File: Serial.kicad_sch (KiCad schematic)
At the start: 19 parts

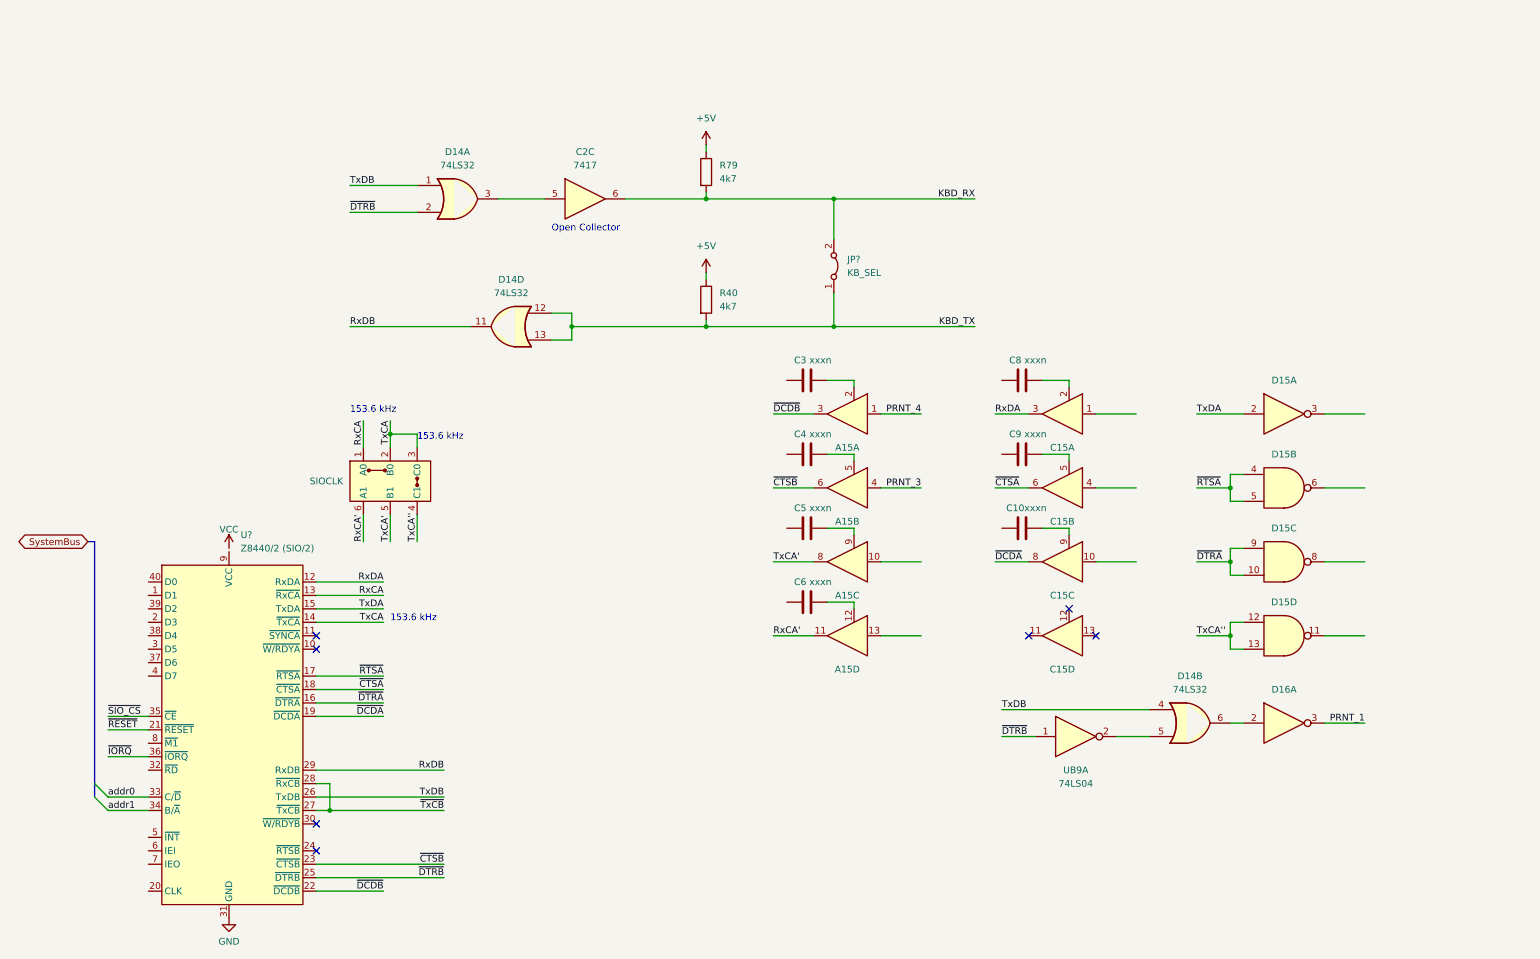
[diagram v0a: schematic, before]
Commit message: serial: wire renaming
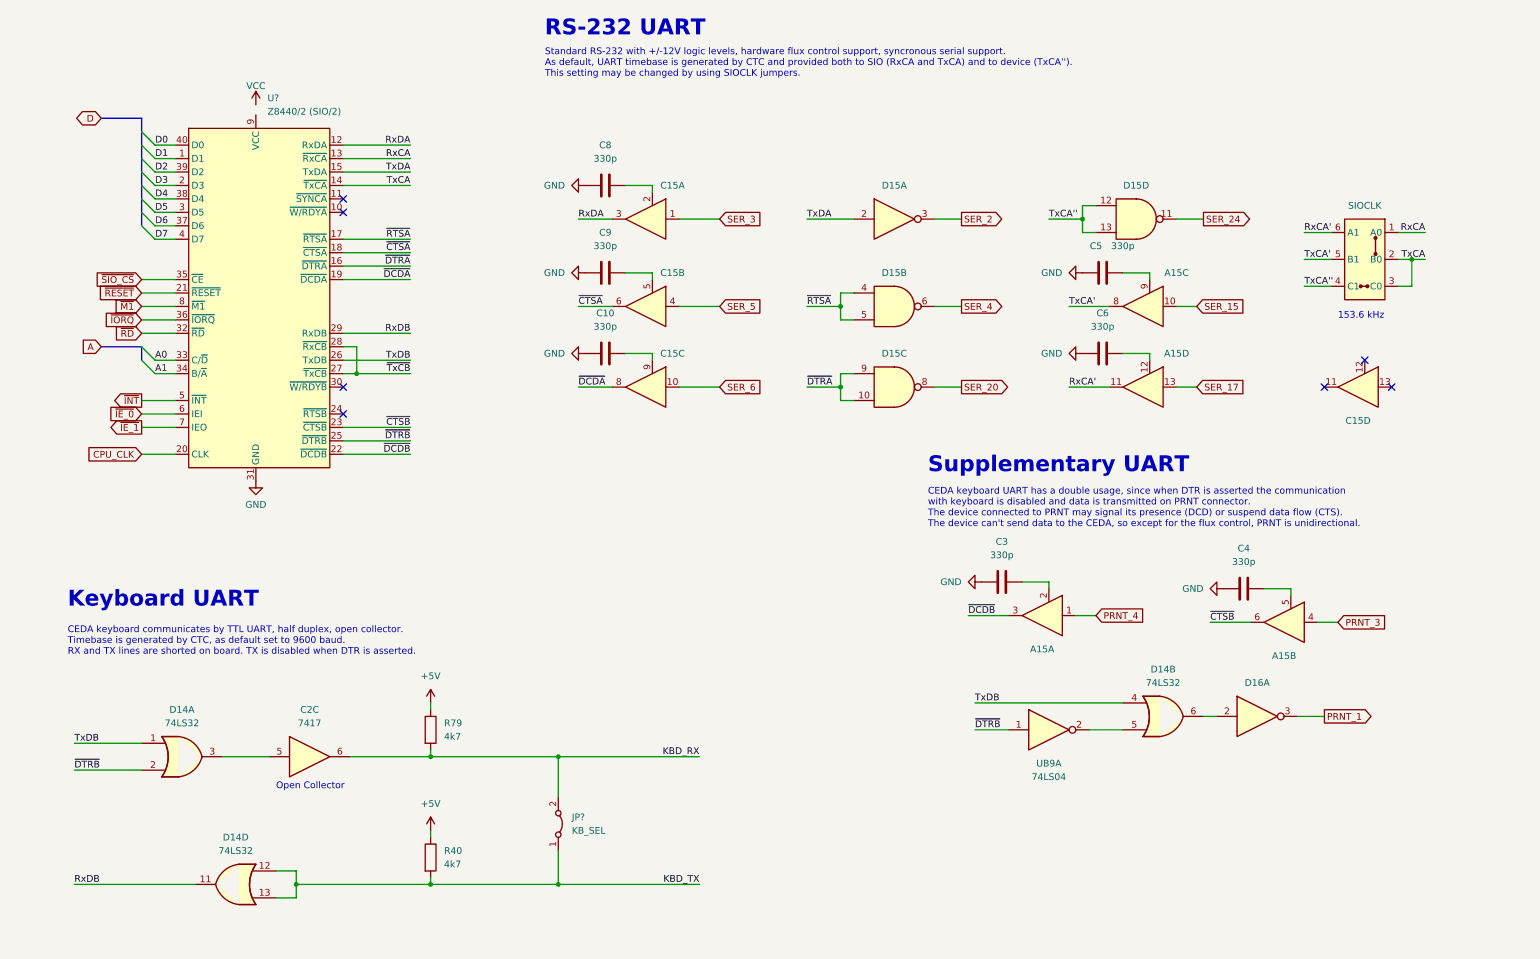
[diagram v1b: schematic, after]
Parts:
- C10, C3, C4, C5, C6, C8, C9: value xxxn -> 330p
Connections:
- net GND: now also C10.1, C3.1, C4.1, C5.1, C6.1, C8.1, C9.1
- net SER_20: now reaches D15.8
- net SER_6: now reaches C15.10
- net SER_17: now reaches A15.13
- net SER_15: now reaches A15.10
- net D1: now reaches U?.1 (D1)
- net D3: now reaches U?.2 (D3)
- net CPU_CLK: now reaches U?.20 (CLK)
- net D5: now reaches U?.3 (D5)
- net ~{RD}: now reaches U?.32 (~{RD})
- net D6: now reaches U?.37 (D6)
- net D4: now reaches U?.38 (D4)
- net D2: now reaches U?.39 (D2)
- net D7: now reaches U?.4 (D7)
- net D0: now reaches U?.40 (D0)
- net ~{INT}: now reaches U?.5 (~{INT})
- net ~{IE_0}: now reaches U?.6 (IEI)
- net ~{IE_1}: now reaches U?.7 (IEO)
- net ~{M1}: now reaches U?.8 (~{M1})
- net SER_2: now reaches D15.3
- net SER_4: now reaches D15.6
- net SER_24: now reaches D15.11
- net SER_5: now reaches C15.4
- net SER_3: now reaches C15.1
- net addr0 renamed A0
- net addr1 renamed A1
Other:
- note added: "CEDA keyboard UART has a double usage, since when DTR is asserted the communication with keyboard is disabled and data is transmitted on PRNT connector. The device connected to PRNT may signal its presence (DCD) or suspend data flow (CTS). The device can't send data to the CEDA, so except for the flux control, PRNT is unidirectional."
- note added: "CEDA keyboard communicates by TTL UART, half duplex, open collector. Timebase is generated by CTC, as default set to 9600 baud. RX and TX lines are shorted on board. TX is disabled when DTR is asserted."
- note added: "Keyboard UART"
- note added: "RS-232 UART"
- note added: "Standard RS-232 with +/-12V logic levels, hardware flux control support, syncronous serial support. As default, UART timebase is generated by CTC and provided both to SIO (RxCA and TxCA) and to device (TxCA''). This setting may be changed by using SIOCLK jumpers."
- note added: "Supplementary UART"
- moved on the sheet: A15A, A15B, A15C, A15D, C10, C15A, C15B, C15C, C15D, C2C, C3, C4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

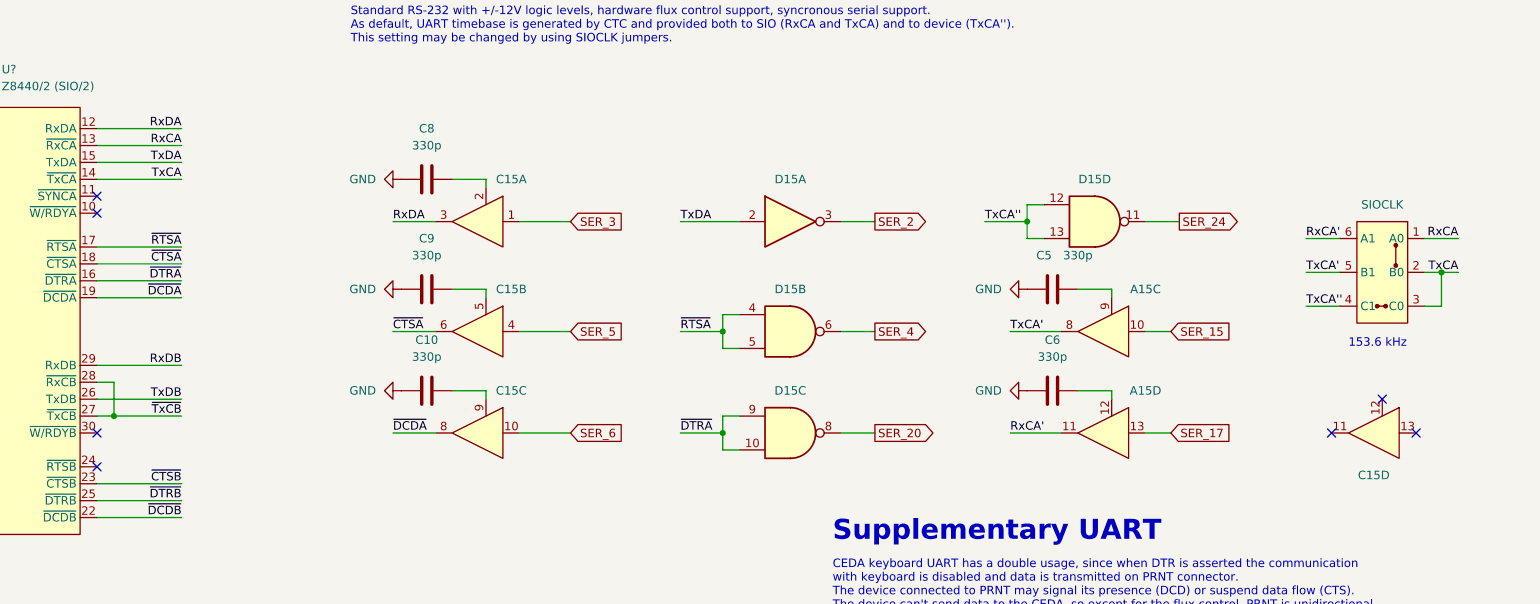
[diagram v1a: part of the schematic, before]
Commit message: Serial: wire renaming
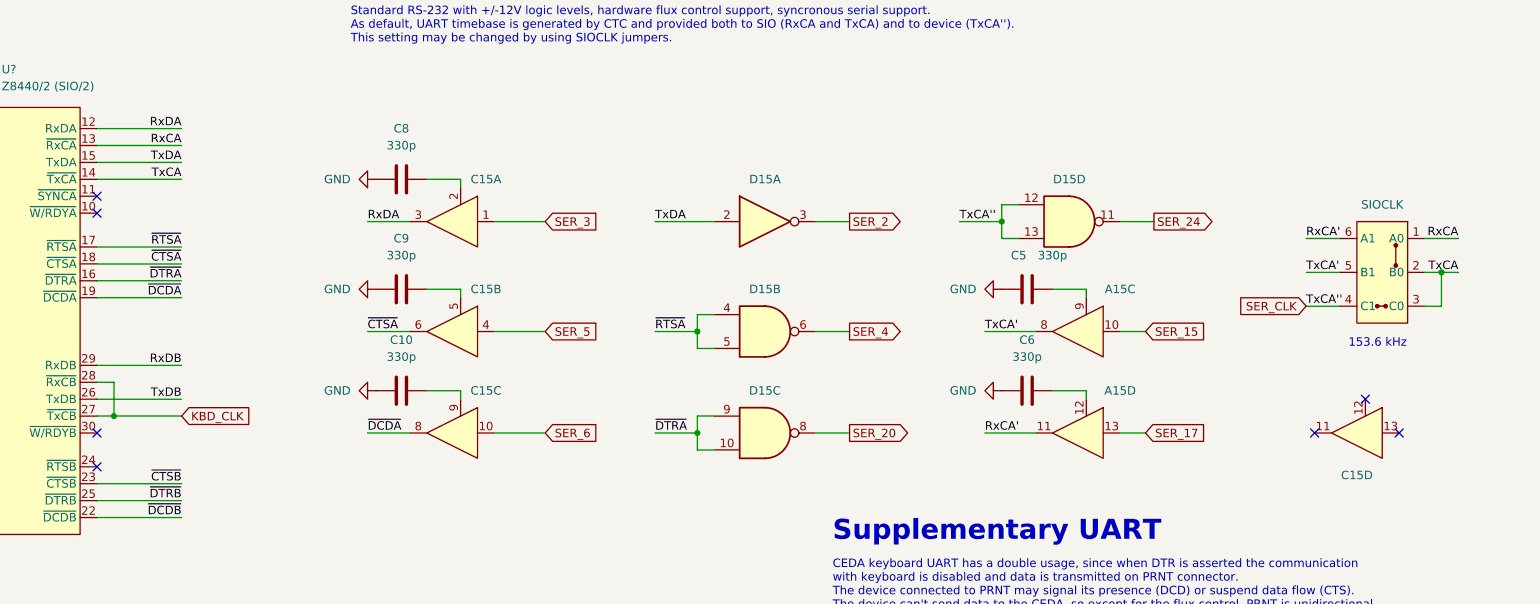
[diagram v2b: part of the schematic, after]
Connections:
- net TxCA'' renamed SER_CLK
- net ~{TxCB} renamed KBD_CLK
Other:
- moved on the sheet: A15C, A15D, C10, C15A, C15B, C15C, C15D, C5, C6, C8, C9, D15A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

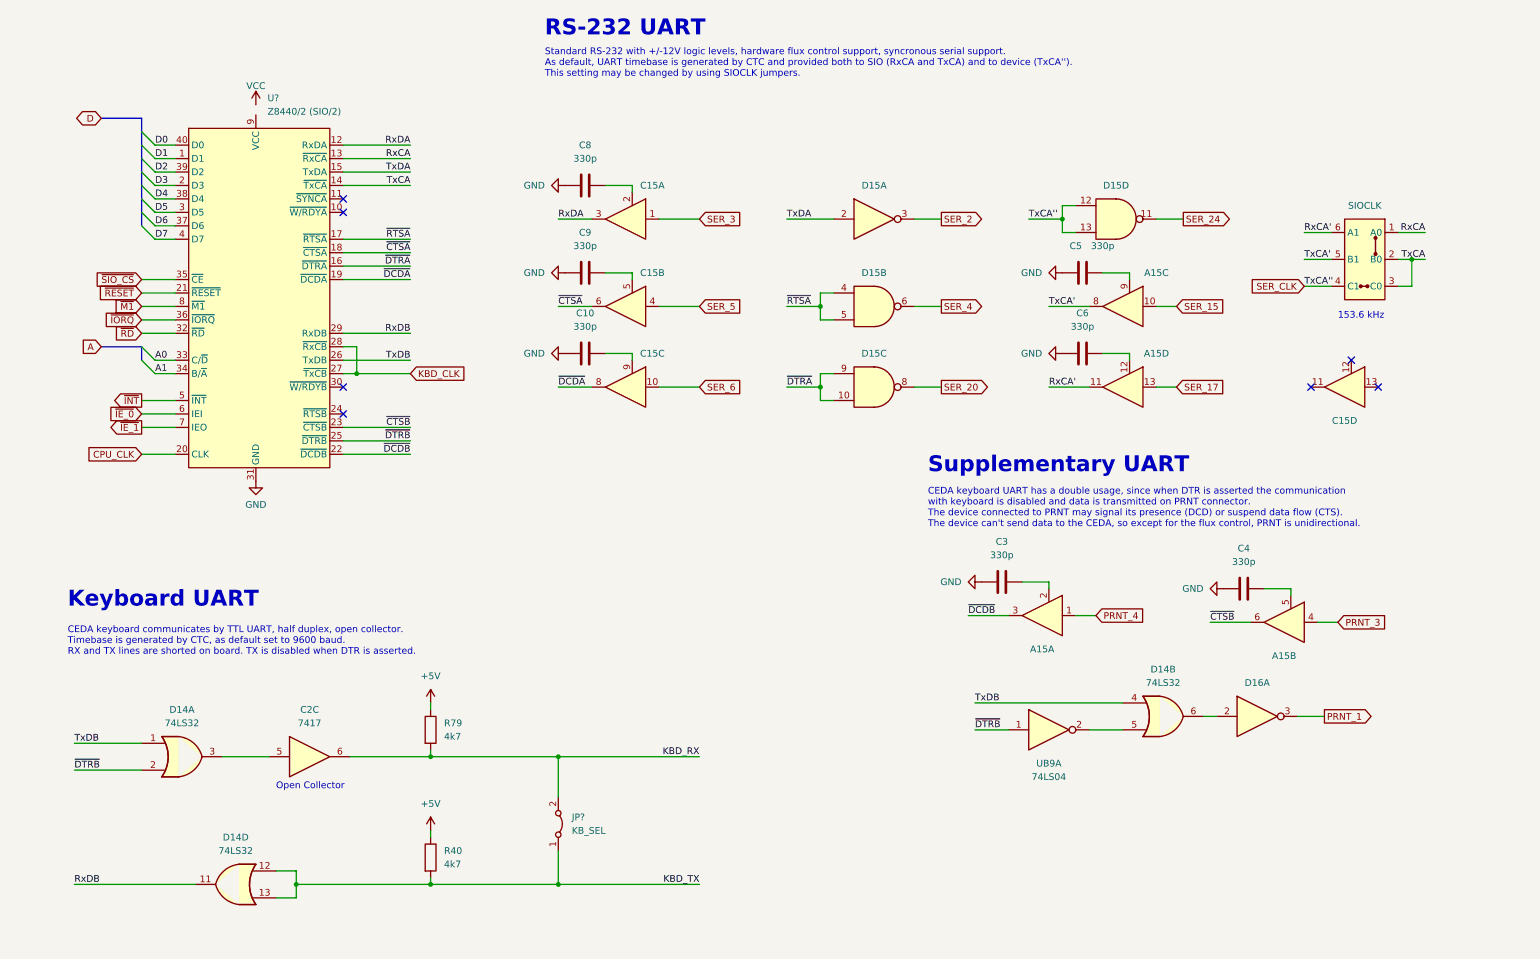
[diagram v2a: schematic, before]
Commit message: Components renaming according to the Uxy convention.
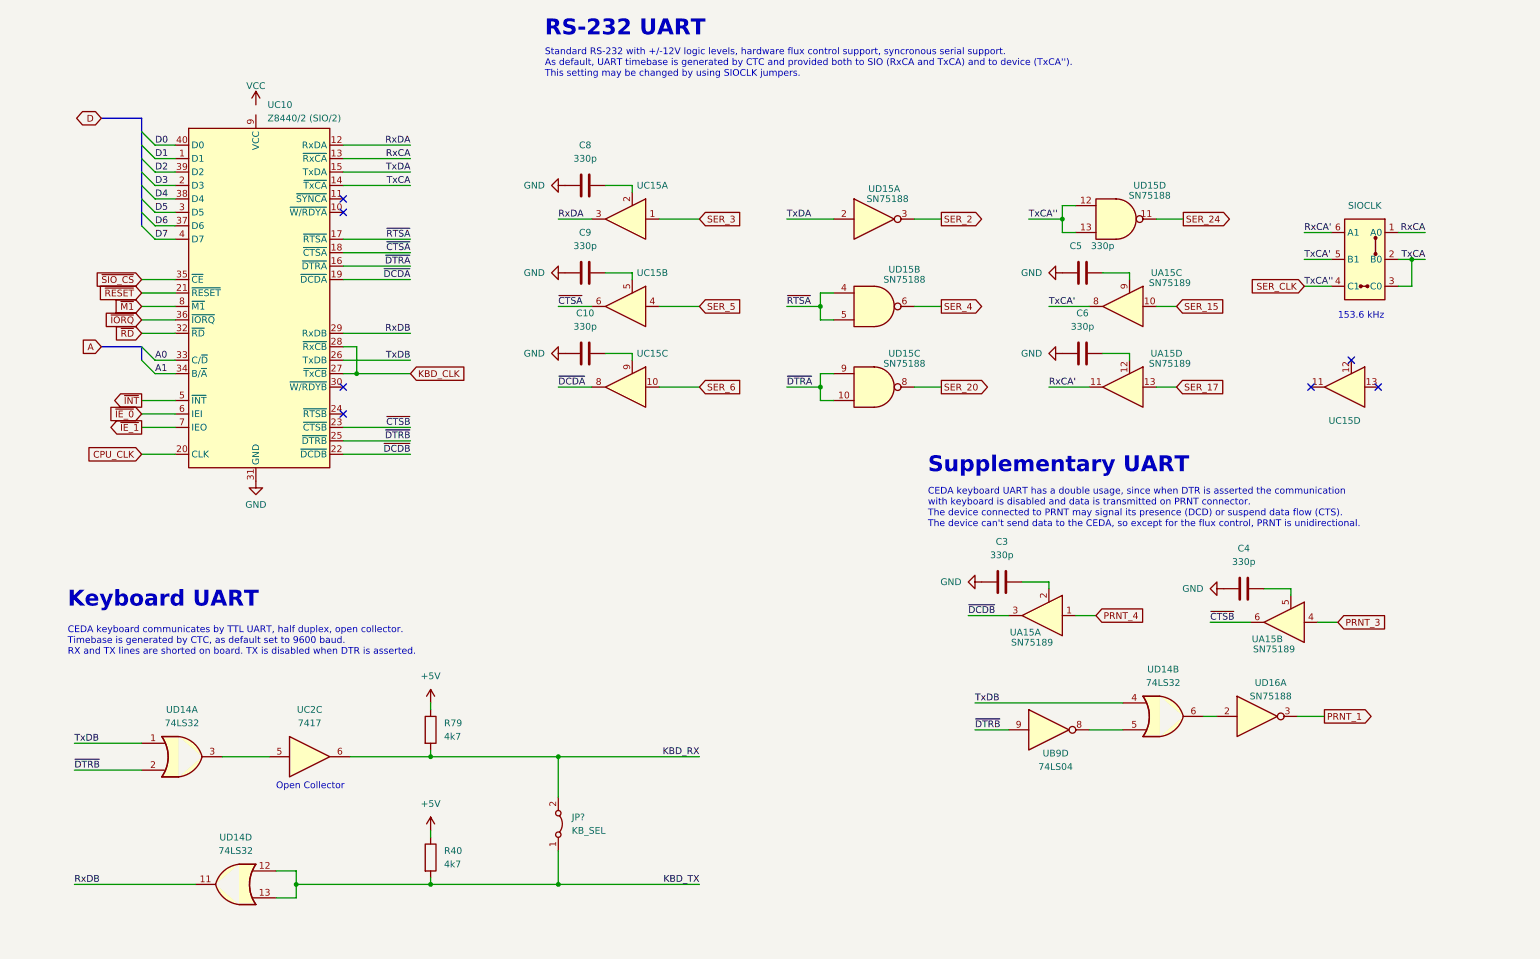
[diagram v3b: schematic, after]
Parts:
- UA15: renamed from A15; value ~ -> SN75189
- UD15: renamed from D15; value ~ -> SN75188
- UD16: renamed from D16; value ~ -> SN75188
- gave numbers to parts that had none: 1
- renumbered C15 to UC15, C2 to UC2, D14 to UD14
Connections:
- net ~{DTRB}: now also UB9.9; no longer UB9.1
- net at UD14.5: now also UB9.8; no longer UB9.2

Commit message: VCC -> +5V
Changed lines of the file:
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@@
     )
   )
-  (symbol (lib_id "power:VCC") (at 58.42 36.83 0) (unit 1)
+  (symbol (lib_name "+5V_1") (lib_id "power:+5V") (at 58.42 36.83 0) (unit 1)
     (in_bom yes) (on_board yes) (dnp no) (fields_autoplaced)
-    (property "Reference" "#PWR0144" (at 58.42 40.64 0)
+    (property "Reference" "#PWR?" (at 58.42 40.64 0)
       (effects (font (size 1.27 1.27)) hide)
     )
-    (property "Value" "VCC" (at 58.42 33.2542 0)
+    (property "Value" "+5V" (at 58.42 31.75 0)
       (effects (font (size 1.27 1.27)))
     )
@@
       (project "ceda"
         (path "/12a6dbe3-008d-4c5b-88f6-9f1c816060be/e6a0e8fd-e32c-428e-9a73-cac8f5494d05"
-          (reference "#PWR0144") (unit 1)
+          (reference "#PWR?") (unit 1)
         )
       )

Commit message: Notes in kicad's sheet text blocks
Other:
- title: FPX-290 -> CEDA - Sanco 8003 schematics
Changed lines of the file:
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@@
   (paper "A4")
   (title_block
-    (title "FPX-290")
+    (title "CEDA - Sanco 8003 schematics")
     (rev "05")
     (company "Logic Systems Int'l Inc")
-    (comment 1 "Serial IO module")
-    (comment 2 "Keyboard, RS-232 compliant port, PRNT port")
+    (comment 1 "reversed by RetrOfficina - retrofficina.glgprograms.it")
+    (comment 2 "an RS232C compliant serial port, a bidirectional parallel port and a further serial port")
+    (comment 3 "Four I/O ports are available: a keyboard port, which is a TTL bidirectional serial, ")
+    (comment 4 "Keyboard, RS-232, parallel port")
   )
   (junction (at 66.04 184.15) (diameter 0) (color 0 0 0 0)

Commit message: Upgrade to KiCAD 9.0
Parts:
- UC10: symbol ceda:Z8440/2 -> ceda:Z8440/2

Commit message: drc: updated symbols
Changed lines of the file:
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@@
 	)
 	(symbol
-		(lib_name "+5V_1")
 		(lib_id "power:+5V")
 		(at 58.42 36.83 0)
@@
 		(dnp no)
 		(fields_autoplaced yes)
-		(property "Reference" "#PWR?"
+		(property "Reference" "#PWR0159"
 			(at 58.42 40.64 0)
 			(effects
@@
 			(project "ceda"
 				(path "/12a6dbe3-008d-4c5b-88f6-9f1c816060be/e6a0e8fd-e32c-428e-9a73-cac8f5494d05"
-					(reference "#PWR?")
+					(reference "#PWR0159")
 					(unit 1)
 				)

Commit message: drc: fixed labels
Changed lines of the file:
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@@
 		)
 	)
-	(global_label "A"
+	(global_label "A[15..0]"
 		(shape input)
 		(at 29.21 82.55 180)
@@
 		)
 		(property "Intersheetrefs" "${INTERSHEET_REFS}"
-			(at 25.1362 82.55 0)
+			(at 18.6047 82.55 0)
 			(effects
 				(font
@@
 		)
 	)
-	(global_label "D"
+	(global_label "D[7..0]"
 		(shape bidirectional)
 		(at 29.21 39.37 180)
@@
 		)
 		(property "Intersheetrefs" "${INTERSHEET_REFS}"
-			(at 23.8435 39.37 0)
+			(at 18.5215 39.37 0)
 			(effects
 				(font
